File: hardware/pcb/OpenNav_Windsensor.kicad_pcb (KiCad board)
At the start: 2 copper layers, 40 x 40 mm, 11 parts, among them IC1 AS5600-ASOT, J1 Conn_01x02_Pin, U1 XIAO-ESP32-C6, U2 StpDwnE3.3-0.5, U3 SS411P, U4 DS18B20

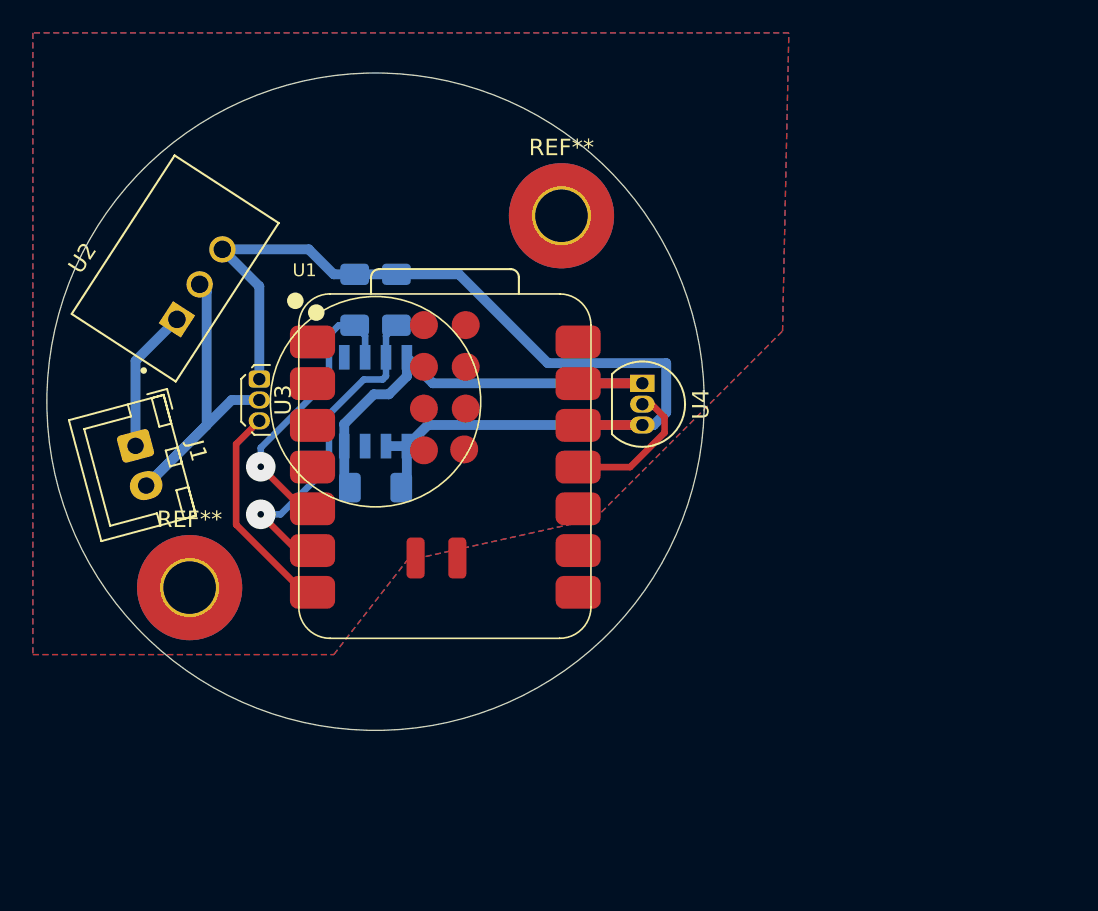
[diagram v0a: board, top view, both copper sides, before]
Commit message: Modified PCB to match Simon's remarks Moved the esp32 to a side, to be able to access the usb port Simplified the routing Made the board more aesthetically pleasing
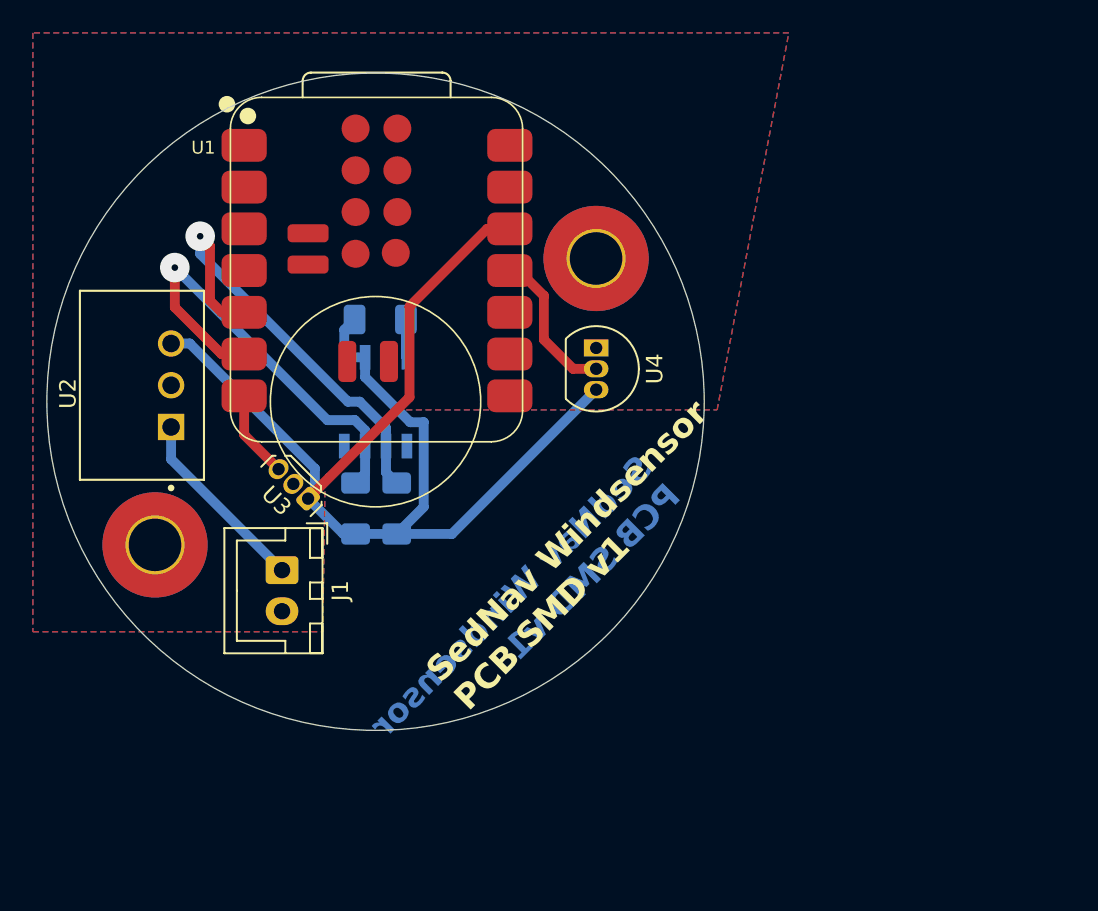
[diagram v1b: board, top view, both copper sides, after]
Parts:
- U1: value XIAO-ESP32-C6 -> XIAO-ESP32-C3/C6/S3
- moved R1 13.0 mm to (134.0, 63.5), turned to -90 degrees
- moved R2 12.9 mm to (131.5, 63.5), turned to -90 degrees
- moved U1 12.7 mm to (133.0, 49.0)
- moved J1 11.7 mm to (127.0, 67.2), turned to -90 degrees
- moved C3 10.2 mm to (133.0, 52.0), turned to 0 degrees
- moved U2 7.39 mm to (118.5, 56.0), turned to 90 degrees
- moved U3 6.70 mm to (127.7, 62.0), turned to 135 degrees
- moved U4 3.54 mm to (146.1, 53.7)
- moved REF** 3.34 mm to (119.3, 65.7)
- moved REF** 3.34 mm to (146.1, 48.3)
- turned IC1 to -90 degrees
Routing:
- net GND: track 52.1 -> 2.32 mm
- net +3.3V: track 66.2 -> 75.5 mm
- net Net-(IC1-SDA): track 18.0 -> 26.9 mm
- net Net-(U1-GPIO16/D6/TX): track 13.3 -> 5.33 mm
- net Net-(IC1-SCL): track 20.4 -> 26.9 mm
- net VCC: track 8.74 -> 11.5 mm
- net Net-(U1-GPIO18/D10/MOSI): track 8.74 -> 9.30 mm
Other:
- board text added: "SedNav Windsensor PCB SMD v1"

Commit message: Added software, corrected for ESP32C6 (untested)
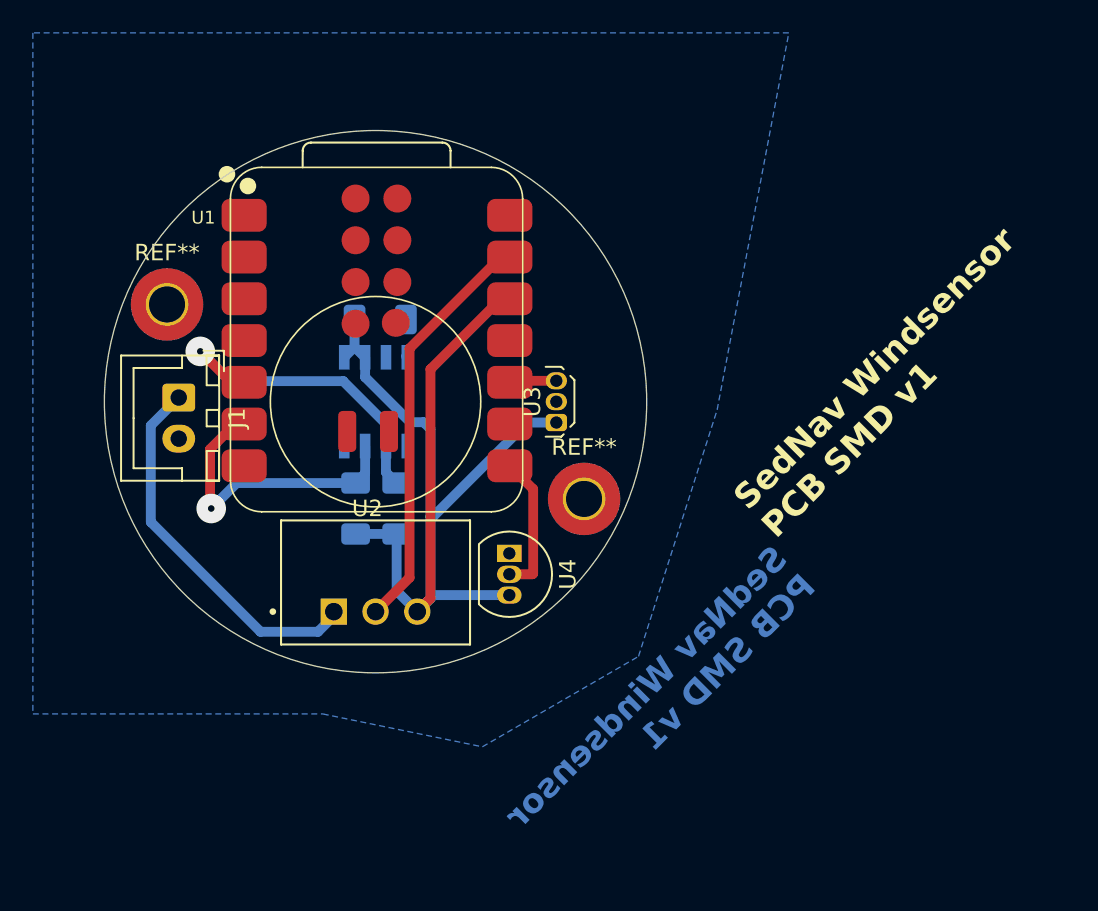
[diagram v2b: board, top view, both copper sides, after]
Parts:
- REF** (x2): value MountingHole_3.2mm_M3_Pad_TopBottom -> MountingHole_2.2mm_M2_Pad_TopBottom; footprint MountingHole:MountingHole_3.2mm_M3_Pad_TopBottom -> MountingHole:MountingHole_2.2mm_M2_Pad_TopBottom
- U1: value XIAO-ESP32-C3/C6/S3 -> XIAO-ESP32-C6
- moved U2 18.6 mm to (132.7, 68.0), turned to 0 degrees
- moved U3 16.8 mm to (143.7, 57.0), turned to 90 degrees
- moved REF** 14.6 mm to (120.0, 51.1)
- moved REF** 14.6 mm to (145.4, 62.9)
- moved U4 13.6 mm to (140.9, 66.2)
- moved J1 12.2 mm to (120.7, 56.8)
- moved U1 4.26 mm to (133.0, 53.3)
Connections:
- U1 pad 10: unconnected-(U1-GPIO20/D9/MISO-Pad10) -> Net-(U1-GPIO20/D9/MISO)
- U1 pad 11: Net-(U1-GPIO18/D10/MOSI) -> unconnected-(U1-GPIO18/D10/MOSI-Pad11)
- U1 pad 7: Net-(U1-GPIO16/D6/TX) -> unconnected-(U1-GPIO16/D6/TX-Pad7)
- U1 pad 8: unconnected-(U1-GPIO17/D7/RX-Pad8) -> Net-(U1-GPIO17/D7/RX)
- U3 pad 3: Net-(U1-GPIO16/D6/TX) -> Net-(U1-GPIO20/D9/MISO)
- U4 pad 2: Net-(U1-GPIO18/D10/MOSI) -> Net-(U1-GPIO17/D7/RX)
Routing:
- net GND: track 2.32 -> 26.5 mm
- net VCC: track 11.5 -> 22.8 mm
- net Net-(U1-GPIO18/D10/MOSI): track 9.30 -> 0.00 mm
- net Net-(IC1-SCL): track 26.9 -> 18.3 mm
- net Net-(U1-GPIO17/D7/RX): track 0.00 -> 8.66 mm
- net +3.3V: track 75.5 -> 66.9 mm
- net Net-(IC1-SDA): track 26.9 -> 21.0 mm
- net Net-(U1-GPIO16/D6/TX): track 5.33 -> 0.00 mm
- net Net-(U1-GPIO20/D9/MISO): track 0.00 -> 2.87 mm
- net unconnected-(U1-GPIO18/D10/MOSI-Pad11): track 0.00 -> 0.54 mm
- removed copper zone on F.Cu, net GND
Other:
- board size 40 x 40 mm -> 33 x 33 mm
